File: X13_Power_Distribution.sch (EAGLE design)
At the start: 35 parts

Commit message: layout!
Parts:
- removed BACKPLANE_SMBUS: (no value), SparkFun-Connectors:CONN_05X2PTH
- removed U$3: NMOSFET-DPAK, MotherboardParts:NMOSFET-DPAK
- added C1, C2, C3: (no value), capacitor-wima:C2.5/4
- added Q1: 310mA/60V/1.6Ω, SparkFun-DiscreteSemi:MOSFET-NCH-2N7002PW
- added U1, U2: Value, Dist_OR_Controller:DIST_OR_DIODE
- CONVERSION_L: device SparkFun-Connectors:CONN_05 -> SparkFun-Connectors:CONN_04
- CONVERSION_R: device SparkFun-Connectors:CONN_05 -> SparkFun-Connectors:CONN_04X2
- D2: device diode:ZENER-DIODESOT23 -> SparkFun-DiscreteSemi:DIODE-ZENER-BZT52C3V6S
- U$1, U$2: value DIODE -> IRF1018EPBF; device DIODE:DIODE -> Reverse_Voltage_NMOS:IRF1018EPBF
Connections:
- removed net 48_GND: U$6.S
- new net 5V_GND: CONVERSION_R.5, CONVERSION_R.6, CONVERSION_R.7, CONVERSION_R.8
- new net N$10: U$1.G, U1.GATE_DRIVE, U1.GATE_PULL_DOWN
- new net N$13: U$2.G, U2.GATE_DRIVE, U2.GATE_PULL_DOWN
- new net N$5: C2.1, U2.VCAPH
- new net N$6: C2.2, U2.VCAPL
- new net N$7: C1.2, U1.VCAPL
- new net N$9: C1.1, U1.VCAPH
- net +12V: now also C3.1, U$1.D, U$2.D, U1.CATHODE, U2.CATHODE; no longer U$1.OUT, U$2.OUT
- net +12V_A: now also U$1.S, U1.ANODE; no longer U$1.IN2
- net +12V_B: now also U$2.S, U2.ANODE; no longer U$2.IN2
- net +3.3V: now also CONVERSION_R.3; no longer BACKPLANE_SMBUS.9, CONVERSION_R.5
- net +48V: now also CONVERSION_L.3, CONVERSION_L.4; no longer CONVERSION_L.5
- net +5V: no longer BACKPLANE_SMBUS.1, BACKPLANE_SMBUS.3, BACKPLANE_SMBUS.5, BACKPLANE_SMBUS.7, CONVERSION_R.3
- net 12V_GND: now also C3.2
- net 48V_GND: now also Q1.S, U$6.S; no longer CONVERSION_L.3, CONVERSION_L.4, U$3.S
- net ALERT: no longer BACKPLANE_SMBUS.4
- net C2_1: no longer BACKPLANE_SMBUS.8
- net C2_2: no longer BACKPLANE_SMBUS.10
- net CLK: no longer BACKPLANE_SMBUS.6
- net DATA: no longer BACKPLANE_SMBUS.2
- net N$2: now also Q1.G; no longer U$3.G
- net ON/OFF: now also Q1.D; no longer U$3.D1
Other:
- note removed: "OR-ING DIODES"
- moved on the sheet: BACKPLANE_GND_1, BACKPLANE_GND_2, BACKPLANE_PWR_1, BACKPLANE_PWR_2, D5, R5

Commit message: Design review time
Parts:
- added BACKPLANE_SIMBUS: 2X6 FEMALE, SparkFun-Connectors:CONN_06X2PTH_FEMALE
- TETHER: value DIST_TO_TETHER -> 48V
- renumbered 48V_TETHER to TETHER
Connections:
- new net ALERT_1: BACKPLANE_SIMBUS.4
- new net ALERT_2: BACKPLANE_SIMBUS.6
- new net N$4: BACKPLANE_SIMBUS.11, BACKPLANE_SIMBUS.9
- net +3.3V: now also BACKPLANE_SIMBUS.7
- net +5V: now also BACKPLANE_SIMBUS.1, BACKPLANE_SIMBUS.3, BACKPLANE_SIMBUS.5
- net C2_1: now also BACKPLANE_SIMBUS.10
- net C2_2: now also BACKPLANE_SIMBUS.12
- net CLK: now also BACKPLANE_SIMBUS.8
- net DATA: now also BACKPLANE_SIMBUS.2
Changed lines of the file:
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@@
 <classes>
 <class number="0" name="default" width="0" drill="0">
+<clearance class="0" value="0.205"/>
 </class>
 </classes>
@@
 <part name="BRICK1_VOUT(-)" library="SparkFun-Connectors" library_urn="urn:adsk.eagle:library:513" deviceset="CONN_08X2" device="" package3d_urn="urn:adsk.eagle:package:38152/1"/>
 <part name="BRICK1_VOUT(+)" library="SparkFun-Connectors" library_urn="urn:adsk.eagle:library:513" deviceset="CONN_08X2" device="" package3d_urn="urn:adsk.eagle:package:38152/1"/>
-<part name="48V_TETHER" library="Dist_To_Tether_Connector" deviceset="DIST_TO_TETHER" device=""/>
 <part name="48V_POE" library="Dist_POE" deviceset="POE_TERMINAL" device=""/>
 <part name="FRAME2" library="SparkFun-Aesthetics" library_urn="urn:adsk.eagle:library:507" deviceset="FRAME-A4L" device=""/>
@@
 <part name="D2" library="SparkFun-DiscreteSemi" library_urn="urn:adsk.eagle:library:514" deviceset="DIODE-ZENER" device="-BZT52C3V6S" package3d_urn="urn:adsk.eagle:package:38441/1" value="5V"/>
 <part name="Q1" library="SparkFun-DiscreteSemi" library_urn="urn:adsk.eagle:library:514" deviceset="MOSFET-NCH" device="-2N7002PW" package3d_urn="urn:adsk.eagle:package:38456/1" value="310mA/60V/1.6Ω"/>
+<part name="TETHER" library="Dist_To_Tether_Connector" deviceset="DIST_TO_TETHER" device="" value="48V"/>
+<part name="BACKPLANE_SIMBUS" library="SparkFun-Connectors" library_urn="urn:adsk.eagle:library:513" deviceset="CONN_06X2" device="PTH_FEMALE" package3d_urn="urn:adsk.eagle:package:38277/1" value="2X6 FEMALE"/>
 </parts>
 <sheets>
@@
 <attribute name="NAME" x="69.85" y="110.998" size="1.778" layer="95" font="vector"/>
 </instance>
-<instance part="48V_TETHER" gate="A" x="15.24" y="162.56" smashed="yes" rot="MR0">
-<attribute name="NAME" x="19.9644" y="174.2186" size="2.0828" layer="95" ratio="6" rot="SMR0"/>
-</instance>
 <instance part="48V_POE" gate="A" x="15.24" y="137.16" smashed="yes" rot="MR0">
 <attribute name="NAME" x="19.9644" y="143.7386" size="2.0828" layer="95" ratio="6" rot="SMR0"/>
@@
 <attribute name="NAME" x="151.13" y="146.05" size="1.778" layer="95" font="vector"/>
 <attribute name="VALUE" x="151.13" y="143.51" size="1.778" layer="96" font="vector"/>
+</instance>
+<instance part="TETHER" gate="A" x="15.24" y="162.56" smashed="yes" rot="MR0">
+<attribute name="NAME" x="19.9644" y="174.2186" size="2.0828" layer="95" ratio="6" rot="SMR0"/>
+</instance>
+<instance part="BACKPLANE_SIMBUS" gate="G$1" x="156.21" y="58.42" smashed="yes">
+<attribute name="NAME" x="154.94" y="74.168" size="1.778" layer="95" font="vector"/>
 </instance>
 </instances>
@@
 <junction x="27.94" y="166.37"/>
 <label x="27.94" y="166.37" size="1.778" layer="95" rot="MR180" xref="yes"/>
-<pinref part="48V_TETHER" gate="A" pin="1"/>
-<pinref part="48V_TETHER" gate="A" pin="2"/>
-<pinref part="48V_TETHER" gate="A" pin="3"/>
+<pinref part="TETHER" gate="A" pin="1"/>
+<pinref part="TETHER" gate="A" pin="2"/>
+<pinref part="TETHER" gate="A" pin="3"/>
 </segment>
 </net>
@@
 </segment>
 <segment>
-<wire x1="246.38" y1="27.94" x2="243.84" y2="27.94" width="0.1524" layer="91"/>
-<label x="246.38" y="27.94" size="0.8128" layer="95" xref="yes"/>
+<wire x1="168.91" y1="63.5" x2="166.37" y2="63.5" width="0.1524" layer="91"/>
+<label x="168.91" y="63.5" size="0.8128" layer="95" xref="yes"/>
+<pinref part="BACKPLANE_SIMBUS" gate="G$1" pin="8"/>
 </segment>
 <segment>
@@
 </segment>
 <segment>
-<wire x1="246.38" y1="35.56" x2="243.84" y2="35.56" width="0.1524" layer="91"/>
-<label x="246.38" y="35.56" size="0.8128" layer="95" xref="yes"/>
+<wire x1="168.91" y1="71.12" x2="166.37" y2="71.12" width="0.1524" layer="91"/>
+<label x="168.91" y="71.12" size="0.8128" layer="95" xref="yes"/>
+<pinref part="BACKPLANE_SIMBUS" gate="G$1" pin="2"/>
 </segment>
 </net>
 <net name="+5V" class="0">
 <segment>
-<wire x1="226.06" y1="35.56" x2="228.6" y2="35.56" width="0.1524" layer="91"/>
-<wire x1="226.06" y1="35.56" x2="226.06" y2="33.02" width="0.1524" layer="91"/>
-<wire x1="226.06" y1="33.02" x2="226.06" y2="30.48" width="0.1524" layer="91"/>
-<wire x1="226.06" y1="30.48" x2="228.6" y2="30.48" width="0.1524" layer="91"/>
-<wire x1="226.06" y1="33.02" x2="228.6" y2="33.02" width="0.1524" layer="91"/>
-<junction x="226.06" y="33.02"/>
-<label x="226.06" y="35.56" size="0.8128" layer="95" rot="R180" xref="yes"/>
+<wire x1="148.59" y1="71.12" x2="151.13" y2="71.12" width="0.1524" layer="91"/>
+<wire x1="148.59" y1="71.12" x2="148.59" y2="68.58" width="0.1524" layer="91"/>
+<wire x1="148.59" y1="68.58" x2="148.59" y2="66.04" width="0.1524" layer="91"/>
+<wire x1="148.59" y1="66.04" x2="151.13" y2="66.04" width="0.1524" layer="91"/>
+<wire x1="148.59" y1="68.58" x2="151.13" y2="68.58" width="0.1524" layer="91"/>
+<junction x="148.59" y="68.58"/>
+<label x="148.59" y="71.12" size="0.8128" layer="95" rot="R180" xref="yes"/>
+<pinref part="BACKPLANE_SIMBUS" gate="G$1" pin="5"/>
+<pinref part="BACKPLANE_SIMBUS" gate="G$1" pin="3"/>
+<pinref part="BACKPLANE_SIMBUS" gate="G$1" pin="1"/>
 </segment>
 <segment>
@@
 <net name="+3.3V" class="0">
 <segment>
-<wire x1="226.06" y1="27.94" x2="228.6" y2="27.94" width="0.1524" layer="91"/>
-<label x="226.06" y="27.94" size="0.8128" layer="95" rot="R180" xref="yes"/>
+<wire x1="148.59" y1="63.5" x2="151.13" y2="63.5" width="0.1524" layer="91"/>
+<label x="148.59" y="63.5" size="0.8128" layer="95" rot="R180" xref="yes"/>
+<pinref part="BACKPLANE_SIMBUS" gate="G$1" pin="7"/>
 </segment>
 <segment>
@@
 <junction x="27.94" y="158.75"/>
 <label x="27.94" y="158.75" size="1.778" layer="95" rot="MR180" xref="yes"/>
-<pinref part="48V_TETHER" gate="A" pin="4"/>
-<pinref part="48V_TETHER" gate="A" pin="5"/>
-<pinref part="48V_TETHER" gate="A" pin="6"/>
+<pinref part="TETHER" gate="A" pin="4"/>
+<pinref part="TETHER" gate="A" pin="5"/>
+<pinref part="TETHER" gate="A" pin="6"/>
 </segment>
 <segment>
@@
 </segment>
 <segment>
-<wire x1="246.38" y1="22.86" x2="243.84" y2="22.86" width="0.1524" layer="91"/>
-<label x="246.38" y="22.86" size="0.8128" layer="95" xref="yes"/>
+<wire x1="168.91" y1="58.42" x2="166.37" y2="58.42" width="0.1524" layer="91"/>
+<label x="168.91" y="58.42" size="0.8128" layer="95" xref="yes"/>
+<pinref part="BACKPLANE_SIMBUS" gate="G$1" pin="12"/>
 </segment>
 </net>
@@
 </segment>
 <segment>
-<wire x1="246.38" y1="25.4" x2="243.84" y2="25.4" width="0.1524" layer="91"/>
-<label x="246.38" y="25.4" size="0.8128" layer="95" xref="yes"/>
+<wire x1="168.91" y1="60.96" x2="166.37" y2="60.96" width="0.1524" layer="91"/>
+<label x="168.91" y="60.96" size="0.8128" layer="95" xref="yes"/>
+<pinref part="BACKPLANE_SIMBUS" gate="G$1" pin="10"/>
 </segment>
 </net>
@@
 <net name="ALERT_2" class="0">
 <segment>
-<wire x1="243.84" y1="30.48" x2="246.38" y2="30.48" width="0.1524" layer="91"/>
-<label x="246.38" y="30.48" size="0.8128" layer="95" xref="yes"/>
+<wire x1="166.37" y1="66.04" x2="168.91" y2="66.04" width="0.1524" layer="91"/>
+<label x="168.91" y="66.04" size="0.8128" layer="95" xref="yes"/>
+<pinref part="BACKPLANE_SIMBUS" gate="G$1" pin="6"/>
 </segment>
 </net>
 <net name="ALERT_1" class="0">
 <segment>
-<wire x1="246.38" y1="33.02" x2="243.84" y2="33.02" width="0.1524" layer="91"/>
-<label x="246.38" y="33.02" size="0.8128" layer="95" xref="yes"/>
+<wire x1="168.91" y1="68.58" x2="166.37" y2="68.58" width="0.1524" layer="91"/>
+<label x="168.91" y="68.58" size="0.8128" layer="95" xref="yes"/>
+<pinref part="BACKPLANE_SIMBUS" gate="G$1" pin="4"/>
 </segment>
 </net>
 <net name="N$4" class="0">
 <segment>
-<wire x1="228.6" y1="25.4" x2="226.06" y2="25.4" width="0.1524" layer="91"/>
-<wire x1="226.06" y1="25.4" x2="226.06" y2="22.86" width="0.1524" layer="91"/>
-<wire x1="226.06" y1="22.86" x2="228.6" y2="22.86" width="0.1524" layer="91"/>
-</segment>
-</net>
+<wire x1="151.13" y1="60.96" x2="148.59" y2="60.96" width="0.1524" layer="91"/>
+<wire x1="148.59" y1="60.96" x2="148.59" y2="58.42" width="0.1524" layer="91"/>
+<wire x1="148.59" y1="58.42" x2="151.13" y2="58.42" width="0.1524" layer="91"/>
+<pinref part="BACKPLANE_SIMBUS" gate="G$1" pin="9"/>
+<pinref part="BACKPLANE_SIMBUS" gate="G$1" pin="11"/>
+</segment>
+</net>

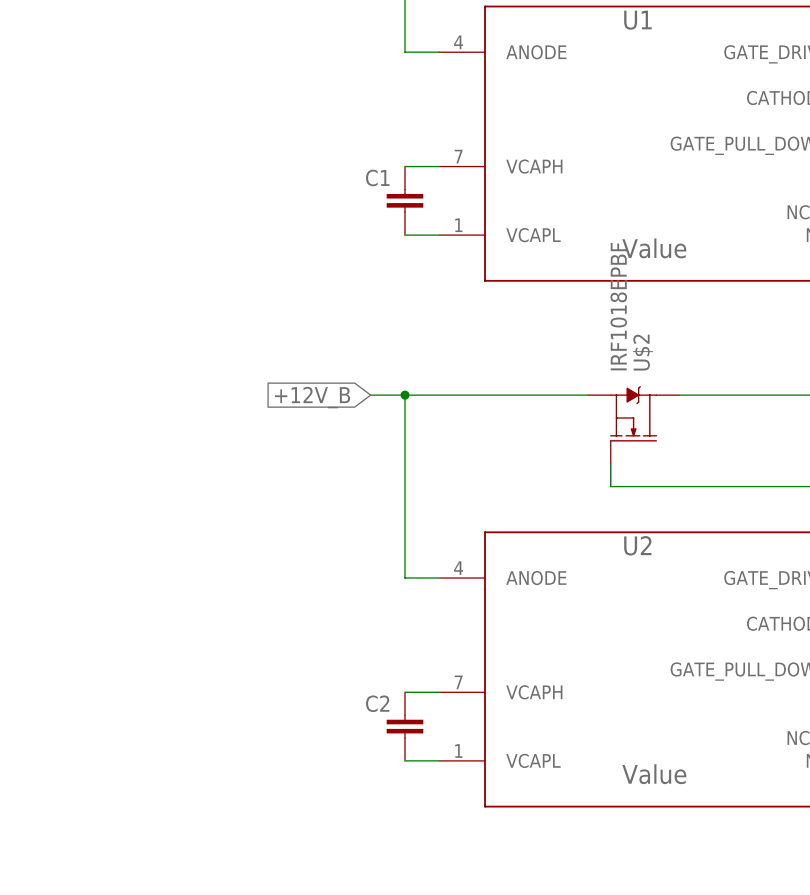
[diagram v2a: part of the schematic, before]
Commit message: cap placeholders fixed
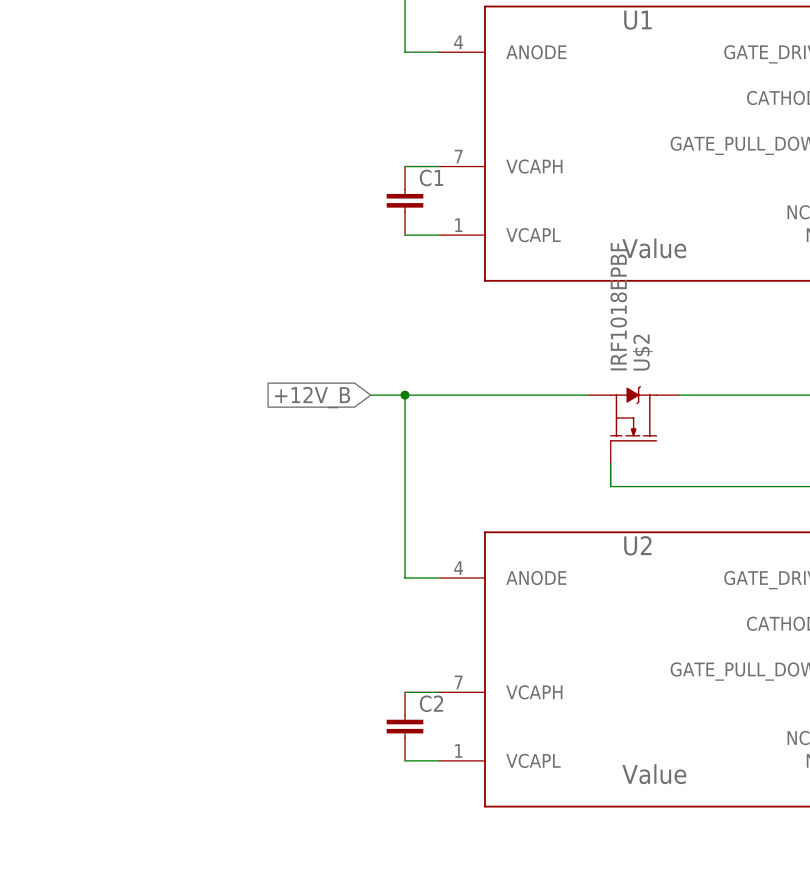
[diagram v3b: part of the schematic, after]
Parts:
- C1, C2, C3: value (none) -> 0.1UF-0603-100V-10%; device capacitor-wima:C2.5/4 -> SparkFun-Capacitors:0.1UF-0603-100V-10%
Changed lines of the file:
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@@
 <part name="U2" library="Dist_OR_Controller" deviceset="DIST_OR_DIODE" device="" value="Value"/>
 <part name="U$1" library="Reverse_Voltage_NMOS" deviceset="IRF1018EPBF" device=""/>
-<part name="C1" library="capacitor-wima" library_urn="urn:adsk.eagle:library:116" deviceset="C" device="2.5/4" package3d_urn="urn:adsk.eagle:package:5408/1"/>
-<part name="C2" library="capacitor-wima" library_urn="urn:adsk.eagle:library:116" deviceset="C" device="2.5/4" package3d_urn="urn:adsk.eagle:package:5408/1"/>
 <part name="U$2" library="Reverse_Voltage_NMOS" deviceset="IRF1018EPBF" device=""/>
-<part name="C3" library="capacitor-wima" library_urn="urn:adsk.eagle:library:116" deviceset="C" device="2.5/4" package3d_urn="urn:adsk.eagle:package:5408/1"/>
 <part name="CONVERSION_L" library="SparkFun-Connectors" library_urn="urn:adsk.eagle:library:513" deviceset="CONN_04" device="" package3d_urn="urn:adsk.eagle:package:38085/1"/>
 <part name="CONVERSION_R" library="SparkFun-Connectors" library_urn="urn:adsk.eagle:library:513" deviceset="CONN_04X2" device="" package3d_urn="urn:adsk.eagle:package:38103/1"/>
@@
 <part name="TETHER" library="Dist_To_Tether_Connector" deviceset="DIST_TO_TETHER" device="" value="48V"/>
 <part name="BACKPLANE_SIMBUS" library="SparkFun-Connectors" library_urn="urn:adsk.eagle:library:513" deviceset="CONN_06X2" device="PTH_FEMALE" package3d_urn="urn:adsk.eagle:package:38277/1" value="2X6 FEMALE"/>
+<part name="C1" library="SparkFun-Capacitors" library_urn="urn:adsk.eagle:library:510" deviceset="0.1UF" device="-0603-100V-10%" package3d_urn="urn:adsk.eagle:package:37414/1" value=""/>
+<part name="C2" library="SparkFun-Capacitors" library_urn="urn:adsk.eagle:library:510" deviceset="0.1UF" device="-0603-100V-10%" package3d_urn="urn:adsk.eagle:package:37414/1" value=""/>
+<part name="C3" library="SparkFun-Capacitors" library_urn="urn:adsk.eagle:library:510" deviceset="0.1UF" device="-0603-100V-10%" package3d_urn="urn:adsk.eagle:package:37414/1" value=""/>
 </parts>
 <sheets>
@@
 <attribute name="VALUE" x="420.37" y="147.32" size="1.778" layer="96" font="vector" rot="MR90"/>
 </instance>
-<instance part="C1" gate="G$1" x="397.51" y="109.22" smashed="yes" rot="MR0">
-<attribute name="NAME" x="395.986" y="109.601" size="1.778" layer="95" rot="MR0"/>
-<attribute name="VALUE" x="395.986" y="104.521" size="1.778" layer="96" rot="MR0"/>
-</instance>
-<instance part="C2" gate="G$1" x="397.51" y="50.8" smashed="yes" rot="MR0">
-<attribute name="NAME" x="395.986" y="51.181" size="1.778" layer="95" rot="MR0"/>
-<attribute name="VALUE" x="395.986" y="46.101" size="1.778" layer="96" rot="MR0"/>
-</instance>
 <instance part="U$2" gate="G$1" x="422.91" y="83.82" smashed="yes" rot="MR90">
 <attribute name="NAME" x="422.91" y="88.9" size="1.778" layer="95" font="vector" rot="MR90"/>
 <attribute name="VALUE" x="420.37" y="88.9" size="1.778" layer="96" font="vector" rot="MR90"/>
 </instance>
-<instance part="C3" gate="G$1" x="459.74" y="50.8" smashed="yes">
-<attribute name="NAME" x="461.264" y="51.181" size="1.778" layer="95"/>
-<attribute name="VALUE" x="461.264" y="46.101" size="1.778" layer="96"/>
-</instance>
 <instance part="CONVERSION_L" gate="G$1" x="196.85" y="162.56" smashed="yes">
 <attribute name="VALUE" x="191.77" y="155.194" size="1.778" layer="96" font="vector"/>
@@
 <instance part="BACKPLANE_SIMBUS" gate="G$1" x="156.21" y="58.42" smashed="yes">
 <attribute name="NAME" x="154.94" y="74.168" size="1.778" layer="95" font="vector"/>
+</instance>
+<instance part="C1" gate="G$1" x="397.51" y="106.68" smashed="yes">
+<attribute name="NAME" x="399.034" y="109.601" size="1.778" layer="95" font="vector"/>
+<attribute name="VALUE" x="399.034" y="104.521" size="1.778" layer="96" font="vector"/>
+</instance>
+<instance part="C2" gate="G$1" x="397.51" y="48.26" smashed="yes">
+<attribute name="NAME" x="399.034" y="51.181" size="1.778" layer="95" font="vector"/>
+<attribute name="VALUE" x="399.034" y="46.101" size="1.778" layer="96" font="vector"/>
+</instance>
+<instance part="C3" gate="G$1" x="459.74" y="48.26" smashed="yes">
+<attribute name="NAME" x="461.264" y="51.181" size="1.778" layer="95" font="vector"/>
+<attribute name="VALUE" x="461.264" y="46.101" size="1.778" layer="96" font="vector"/>
 </instance>
 </instances>
@@
 <wire x1="459.74" y1="86.36" x2="467.36" y2="86.36" width="0.1524" layer="91"/>
 <label x="467.36" y="86.36" size="1.778" layer="95" xref="yes"/>
-<pinref part="C3" gate="G$1" pin="1"/>
 <wire x1="459.74" y1="53.34" x2="459.74" y2="60.96" width="0.1524" layer="91"/>
 <junction x="459.74" y="60.96"/>
+<pinref part="C3" gate="G$1" pin="1"/>
 </segment>
 </net>
@@
 </segment>
 <segment>
-<pinref part="C3" gate="G$1" pin="2"/>
 <wire x1="459.74" y1="45.72" x2="459.74" y2="40.64" width="0.1524" layer="91"/>
 <label x="459.74" y="40.64" size="1.778" layer="95" rot="R270" xref="yes"/>
+<pinref part="C3" gate="G$1" pin="2"/>
 </segment>
 </net>
@@
 <segment>
 <pinref part="U2" gate="A" pin="VCAPH"/>
+<wire x1="401.32" y1="53.34" x2="397.51" y2="53.34" width="0.1524" layer="91"/>
 <pinref part="C2" gate="G$1" pin="1"/>
-<wire x1="401.32" y1="53.34" x2="397.51" y2="53.34" width="0.1524" layer="91"/>
 </segment>
 </net>
 <net name="N$6" class="0">
 <segment>
-<pinref part="C2" gate="G$1" pin="2"/>
 <pinref part="U2" gate="A" pin="VCAPL"/>
 <wire x1="397.51" y1="45.72" x2="401.32" y2="45.72" width="0.1524" layer="91"/>
+<pinref part="C2" gate="G$1" pin="2"/>
 </segment>
 </net>
 <net name="N$7" class="0">
 <segment>
-<pinref part="C1" gate="G$1" pin="2"/>
 <pinref part="U1" gate="A" pin="VCAPL"/>
 <wire x1="397.51" y1="104.14" x2="401.32" y2="104.14" width="0.1524" layer="91"/>
+<pinref part="C1" gate="G$1" pin="2"/>
 </segment>
 </net>
@@
 <segment>
 <pinref part="U1" gate="A" pin="VCAPH"/>
+<wire x1="401.32" y1="111.76" x2="397.51" y2="111.76" width="0.1524" layer="91"/>
 <pinref part="C1" gate="G$1" pin="1"/>
-<wire x1="401.32" y1="111.76" x2="397.51" y2="111.76" width="0.1524" layer="91"/>
-</segment>
-</net>
+</segment>
+</net>

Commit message: 2020/11/21
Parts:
- C3: value 0.1UF-0603-100V-10% -> 330uF; device SparkFun-Capacitors:0.1UF-0603-100V-10% -> brick-capacitor-UCM1H331MNL1GS:UCM1H331MNL1GS
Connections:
- net +12V: now also C3.+; no longer C3.1
- net 12V_GND: now also C3.-; no longer C3.2
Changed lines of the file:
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@@
 <part name="C1" library="SparkFun-Capacitors" library_urn="urn:adsk.eagle:library:510" deviceset="0.1UF" device="-0603-100V-10%" package3d_urn="urn:adsk.eagle:package:37414/1" value=""/>
 <part name="C2" library="SparkFun-Capacitors" library_urn="urn:adsk.eagle:library:510" deviceset="0.1UF" device="-0603-100V-10%" package3d_urn="urn:adsk.eagle:package:37414/1" value=""/>
-<part name="C3" library="SparkFun-Capacitors" library_urn="urn:adsk.eagle:library:510" deviceset="0.1UF" device="-0603-100V-10%" package3d_urn="urn:adsk.eagle:package:37414/1" value=""/>
+<part name="C3" library="brick-capacitor-UCM1H331MNL1GS" deviceset="UCM1H331MNL1GS" device="" package3d_urn="urn:adsk.eagle:package:24202090/2" value="330uF"/>
 </parts>
 <sheets>
@@
 <attribute name="VALUE" x="399.034" y="46.101" size="1.778" layer="96" font="vector"/>
 </instance>
-<instance part="C3" gate="G$1" x="459.74" y="48.26" smashed="yes">
-<attribute name="NAME" x="461.264" y="51.181" size="1.778" layer="95" font="vector"/>
-<attribute name="VALUE" x="461.264" y="46.101" size="1.778" layer="96" font="vector"/>
+<instance part="C3" gate="G$1" x="459.74" y="50.8" smashed="yes">
+<attribute name="NAME" x="461.01" y="52.07" size="1.778" layer="95" align="center-left"/>
+<attribute name="VALUE" x="461.01" y="46.99" size="1.778" layer="95" align="center-left"/>
 </instance>
 </instances>
@@
 <wire x1="459.74" y1="53.34" x2="459.74" y2="60.96" width="0.1524" layer="91"/>
 <junction x="459.74" y="60.96"/>
-<pinref part="C3" gate="G$1" pin="1"/>
+<pinref part="C3" gate="G$1" pin="+"/>
 </segment>
 </net>
@@
 </segment>
 <segment>
-<wire x1="459.74" y1="45.72" x2="459.74" y2="40.64" width="0.1524" layer="91"/>
+<wire x1="459.74" y1="46.355" x2="459.74" y2="40.64" width="0.1524" layer="91"/>
 <label x="459.74" y="40.64" size="1.778" layer="95" rot="R270" xref="yes"/>
-<pinref part="C3" gate="G$1" pin="2"/>
-</segment>
-</net>
+<pinref part="C3" gate="G$1" pin="-"/>
+</segment>
+</net>
